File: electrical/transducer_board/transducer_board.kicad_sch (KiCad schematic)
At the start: 89 parts, among them J1 Conn_01x04_MountingPin, J2 Conn_01x01, J3 Conn_01x01, J4 Conn_01x01, J6 Conn_01x01, J9 Conn_01x01, U1 XL62783, U2 XL62083, U3 XL62783, U4 XL62083, U5 LCMXO3L-2100E-5UWG49, U6 MIC5504-1.2YM5, U7 MIC5504-3.3YM5, U8 74LVC3G34, X1 S3D10.000000B20F30T

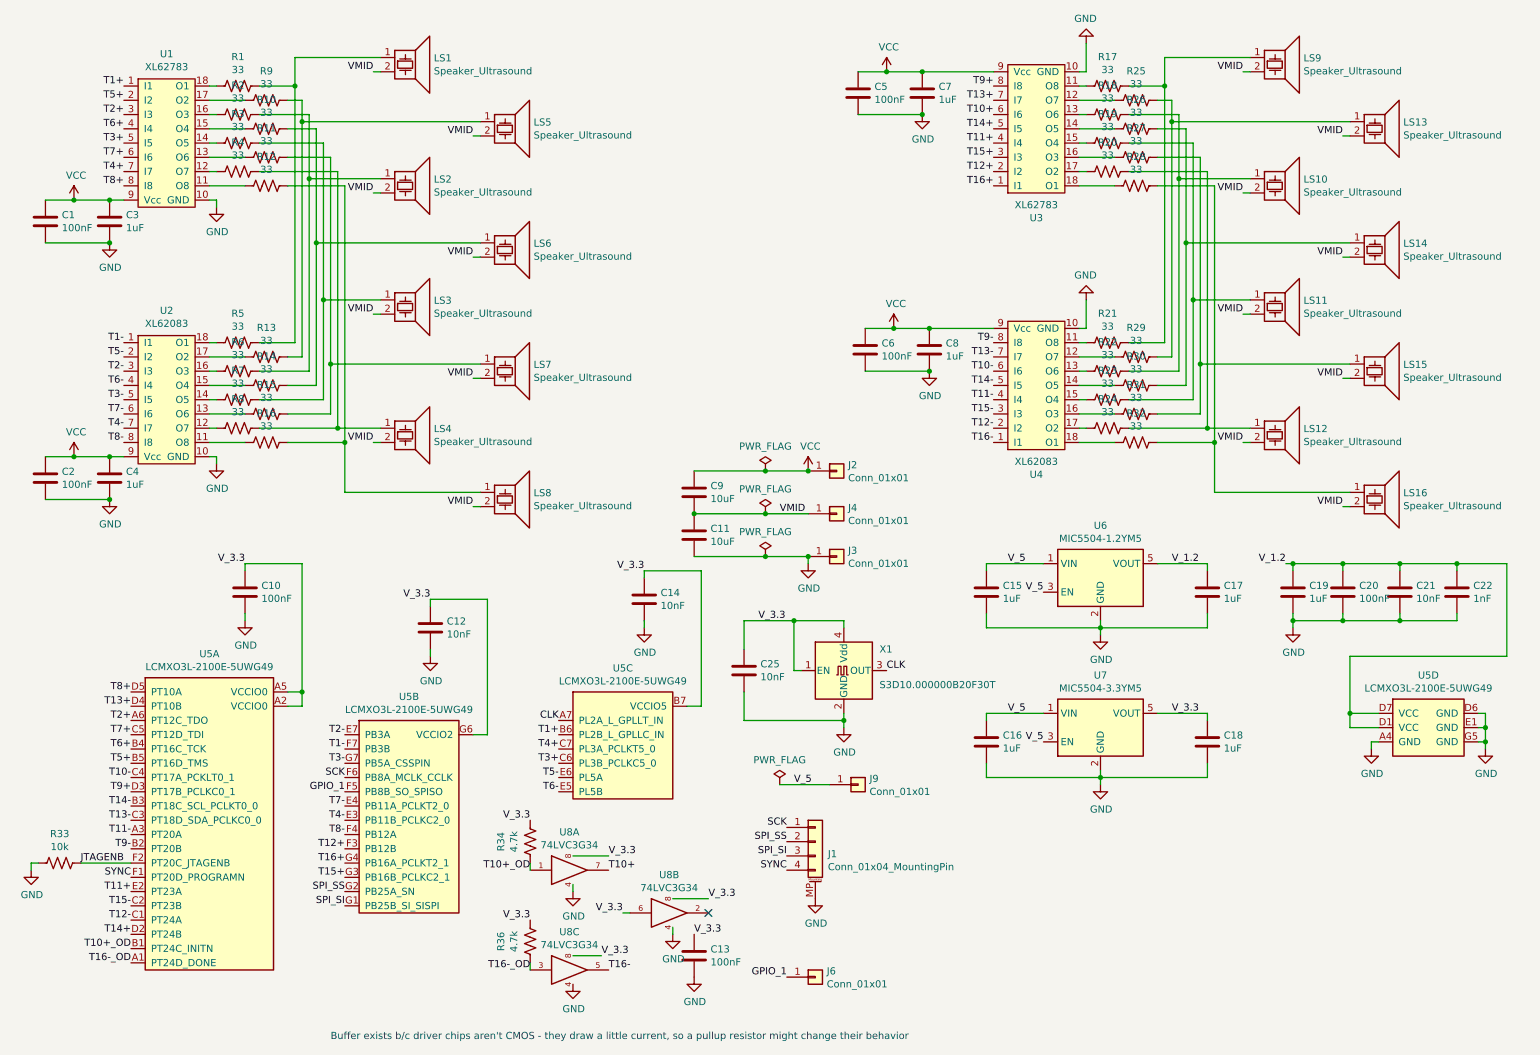
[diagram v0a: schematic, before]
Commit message: Fixed XL62083 pins and made other adjustments
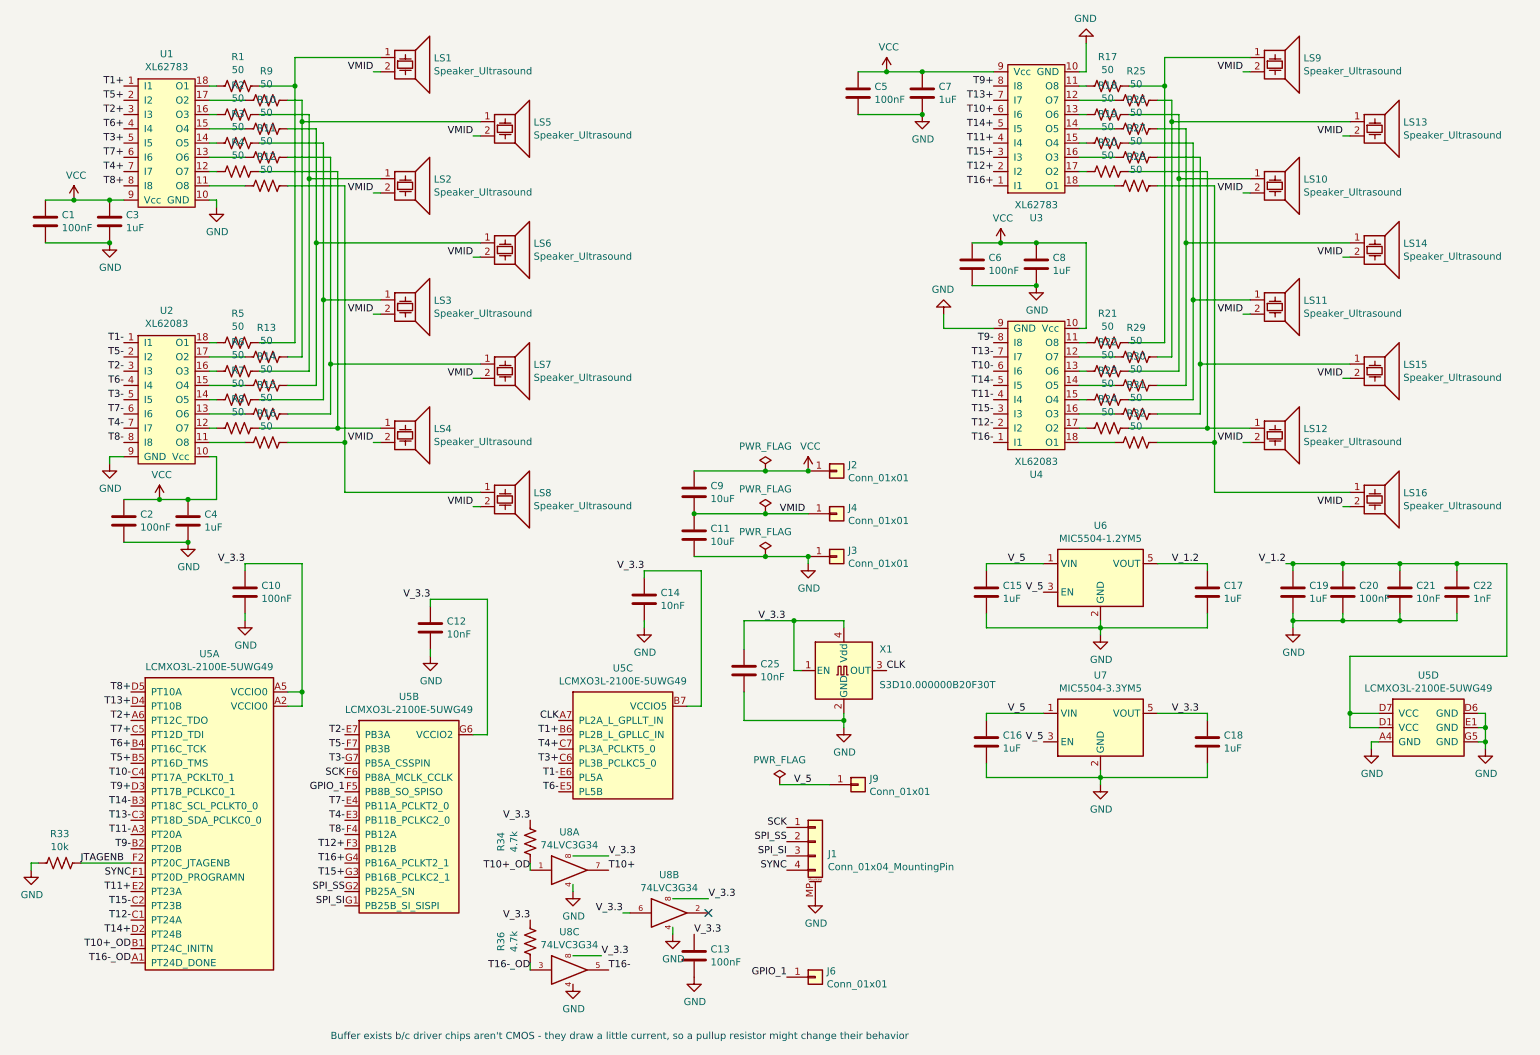
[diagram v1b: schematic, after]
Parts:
- R1, R10, R11, R12, R13, R14, R15, R16, R17, R18, R19, R2, R20, R21, R22, R23, R24, R25, R26, R27, R28, R29, R3, R30, R31, R32, R4, R5, R6, R7, R8, R9: value 33 -> 50
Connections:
- net GND: now also U2.9 (GND), U4.9 (GND); no longer U2.10 (GND), U4.10 (GND)
- net T1-: now also U5.E6 (PL5A); no longer U5.F7 (PB3B)
- net T5-: now also U5.F7 (PB3B); no longer U5.E6 (PL5A)
- net VCC: now also U2.10 (Vcc), U4.10 (Vcc); no longer U2.9 (Vcc), U4.9 (Vcc)
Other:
- moved on the sheet: C2, C4, C6, C8

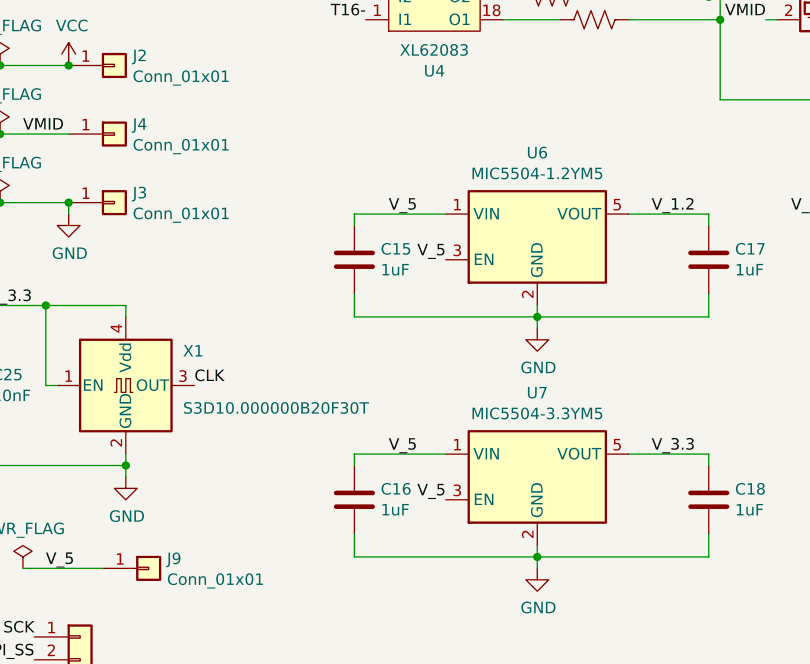
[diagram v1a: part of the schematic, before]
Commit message: Swapped some parts
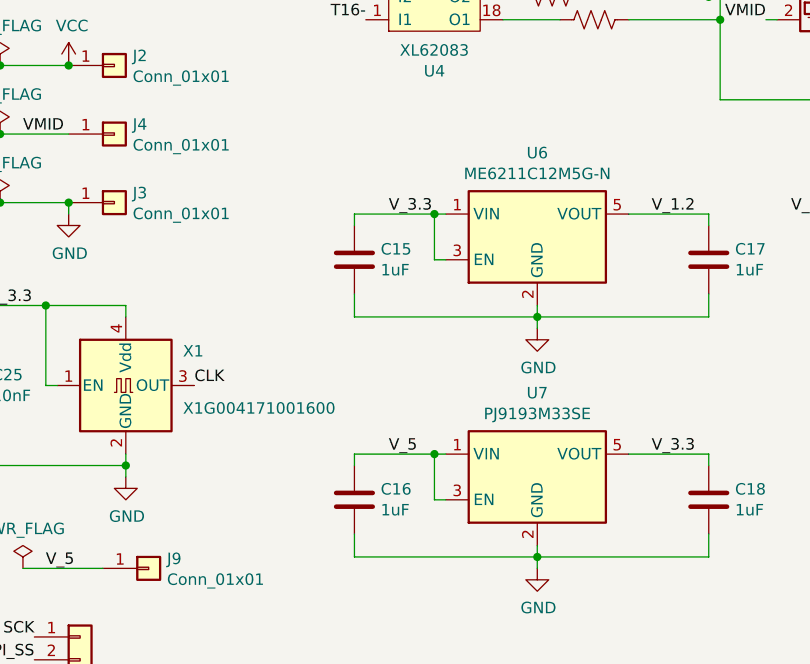
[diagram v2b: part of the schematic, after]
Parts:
- U6: value MIC5504-1.2YM5 -> ME6211C12M5G-N
- U7: value MIC5504-3.3YM5 -> PJ9193M33SE
- X1: value S3D10.000000B20F30T -> X1G004171001600; footprint Oscillator:Oscillator_SMD_Abracon_ASE-4Pin_3.2x2.5mm -> Oscillator:Oscillator_SMD_SeikoEpson_SG210-4Pin_2.5x2.0mm
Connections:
- net V_3.3: now also C15.1, U6.1 (VIN), U6.3 (EN)
- net V_5: no longer C15.1, U6.1 (VIN), U6.3 (EN)
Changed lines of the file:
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@@
   (junction (at 133.35 111.76) (diameter 0) (color 0 0 0 0)
   )
+  (junction (at 194.31 120.65) (diameter 0) (color 0 0 0 0)
+  )
   (junction (at 224.79 96.52) (diameter 0) (color 0 0 0 0)
   )
@@
   (junction (at 43.18 116.84) (diameter 0) (color 0 0 0 0)
   )
+  (junction (at 194.31 147.32) (diameter 0) (color 0 0 0 0)
+  )
   (junction (at 173.99 40.64) (diameter 0) (color 0 0 0 0)
   )
@@
     (stroke (width 0) (type default) (color 0 0 0 0))
   )
+  (wire (pts (xy 194.31 147.32) (xy 194.31 152.4))
+    (stroke (width 0) (type default) (color 0 0 0 0))
+  )
   (wire (pts (xy 64.77 52.07) (xy 77.47 52.07))
     (stroke (width 0) (type default) (color 0 0 0 0))
@@
     (stroke (width 0) (type default) (color 0 0 0 0))
   )
+  (wire (pts (xy 194.31 152.4) (xy 195.58 152.4))
+    (stroke (width 0) (type default) (color 0 0 0 0))
+  )
   (wire (pts (xy 146.05 119.38) (xy 153.67 119.38))
     (stroke (width 0) (type default) (color 0 0 0 0))
@@
     (stroke (width 0) (type default) (color 0 0 0 0))
   )
+  (wire (pts (xy 194.31 120.65) (xy 185.42 120.65))
+    (stroke (width 0) (type default) (color 0 0 0 0))
+  )
   (wire (pts (xy 250.19 66.04) (xy 248.92 66.04))
     (stroke (width 0) (type default) (color 0 0 0 0))
@@
     (stroke (width 0) (type default) (color 0 0 0 0))
   )
+  (wire (pts (xy 194.31 125.73) (xy 195.58 125.73))
+    (stroke (width 0) (type default) (color 0 0 0 0))
+  )
   (wire (pts (xy 223.52 93.98) (xy 223.52 85.09))
     (stroke (width 0) (type default) (color 0 0 0 0))
@@
     (stroke (width 0) (type default) (color 0 0 0 0))
   )
+  (wire (pts (xy 194.31 120.65) (xy 194.31 125.73))
+    (stroke (width 0) (type default) (color 0 0 0 0))
+  )
   (wire (pts (xy 162.56 33.02) (xy 167.64 33.02))
     (stroke (width 0) (type default) (color 0 0 0 0))
@@
     (stroke (width 0) (type default) (color 0 0 0 0))
   )
-  (wire (pts (xy 195.58 120.65) (xy 185.42 120.65))
+  (wire (pts (xy 195.58 120.65) (xy 194.31 120.65))
     (stroke (width 0) (type default) (color 0 0 0 0))
   )
@@
     (stroke (width 0) (type default) (color 0 0 0 0))
   )
-  (wire (pts (xy 185.42 147.32) (xy 195.58 147.32))
+  (wire (pts (xy 185.42 147.32) (xy 194.31 147.32))
     (stroke (width 0) (type default) (color 0 0 0 0))
   )
@@
     (stroke (width 0) (type default) (color 0 0 0 0))
   )
+  (wire (pts (xy 194.31 147.32) (xy 195.58 147.32))
+    (stroke (width 0) (type default) (color 0 0 0 0))
+  )
   (wire (pts (xy 111.76 179.07) (xy 111.76 177.8))
     (stroke (width 0) (type default) (color 0 0 0 0))
@@
     (effects (font (size 1.27 1.27)) (justify right bottom))
   )
-  (label "V_5" (at 189.23 120.65 0)
+  (label "V_3.3" (at 189.23 120.65 0)
     (effects (font (size 1.27 1.27)) (justify left bottom))
   )
@@
     (effects (font (size 1.27 1.27)) (justify right bottom))
   )
-  (label "V_5" (at 195.58 152.4 180)
-    (effects (font (size 1.27 1.27)) (justify right bottom))
-  )
   (label "T10-" (at 186.69 86.36 180)
     (effects (font (size 1.27 1.27)) (justify right bottom))
@@
     (effects (font (size 1.27 1.27)) (justify right bottom))
   )
-  (label "V_5" (at 195.58 125.73 180)
-    (effects (font (size 1.27 1.27)) (justify right bottom))
-  )
   (label "T14+" (at 186.69 43.18 180)
     (effects (font (size 1.27 1.27)) (justify right bottom))
@@
     (in_bom yes) (on_board yes)
     (property "Reference" "U6" (id 0) (at 205.74 113.8682 0))
-    (property "Value" "MIC5504-1.2YM5" (id 1) (at 205.74 116.1796 0))
+    (property "Value" "ME6211C12M5G-N" (id 1) (at 205.74 116.1796 0))
     (property "Footprint" "Package_TO_SOT_SMD:SOT-23-5" (id 2) (at 205.74 133.35 0)
       (effects (font (size 1.27 1.27)) hide)
@@
     (in_bom yes) (on_board yes)
     (property "Reference" "U7" (id 0) (at 205.74 140.5382 0))
-    (property "Value" "MIC5504-3.3YM5" (id 1) (at 205.74 142.8496 0))
+    (property "Value" "PJ9193M33SE" (id 1) (at 205.74 142.8496 0))
     (property "Footprint" "Package_TO_SOT_SMD:SOT-23-5" (id 2) (at 205.74 160.02 0)
       (effects (font (size 1.27 1.27)) hide)
@@
       (effects (font (size 1.27 1.27)) (justify left))
     )
-    (property "Value" "S3D10.000000B20F30T" (id 1) (at 166.37 142.24 0)
+    (property "Value" "X1G004171001600" (id 1) (at 166.37 142.24 0)
       (effects (font (size 1.27 1.27)) (justify left))
     )
-    (property "Footprint" "Oscillator:Oscillator_SMD_Abracon_ASE-4Pin_3.2x2.5mm" (id 2) (at 177.8 148.59 0)
+    (property "Footprint" "Oscillator:Oscillator_SMD_SeikoEpson_SG210-4Pin_2.5x2.0mm" (id 2) (at 177.8 148.59 0)
       (effects (font (size 1.27 1.27)) hide)
     )
@@
     )
     (path "/00000000-0000-0000-0000-0000613404e8"
-      (reference "U6") (unit 1) (value "MIC5504-1.2YM5") (footprint "Package_TO_SOT_SMD:SOT-23-5")
+      (reference "U6") (unit 1) (value "ME6211C12M5G-N") (footprint "Package_TO_SOT_SMD:SOT-23-5")
     )
     (path "/00000000-0000-0000-0000-00006134175c"
-      (reference "U7") (unit 1) (value "MIC5504-3.3YM5") (footprint "Package_TO_SOT_SMD:SOT-23-5")
+      (reference "U7") (unit 1) (value "PJ9193M33SE") (footprint "Package_TO_SOT_SMD:SOT-23-5")
     )
     (path "/00000000-0000-0000-0000-000061572b7c"
@@
     )
     (path "/00000000-0000-0000-0000-00006168392e"
-      (reference "X1") (unit 1) (value "S3D10.000000B20F30T") (footprint "Oscillator:Oscillator_SMD_Abracon_ASE-4Pin_3.2x2.5mm")
+      (reference "X1") (unit 1) (value "X1G004171001600") (footprint "Oscillator:Oscillator_SMD_SeikoEpson_SG210-4Pin_2.5x2.0mm")
     )
   )

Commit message: Add a few components
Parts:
- added C23, C24, C26, C27, C28, C29: (no value), symbol Device:C
- added D1, D2: (no value), symbol Device:D
- C1, C10, C13, C2, C20, C5, C6: value 100nF -> (none); footprint Capacitor_SMD:C_0603_1608Metric -> (none)
- C11, C9: value 10uF -> (none); footprint Capacitor_SMD:C_0805_2012Metric -> (none)
- C12, C14, C25: value 10nF -> (none); footprint Capacitor_SMD:C_0402_1005Metric -> (none)
- C15, C16, C17, C18, C19, C3, C4, C7, C8: value 1uF -> (none); footprint Capacitor_SMD:C_0603_1608Metric -> (none)
- C21: value 10nF -> (none); footprint Capacitor_SMD:C_0603_1608Metric_Pad1.08x0.95mm_HandSolder -> (none)
- C22: value 1nF -> (none); footprint Capacitor_SMD:C_0603_1608Metric_Pad1.08x0.95mm_HandSolder -> (none)
- J1: value Conn_01x04_MountingPin -> (none); footprint Connector_JST:JST_SH_BM04B-SRSS-TB_1x04-1MP_P1.00mm_Vertical -> (none)
- J2, J3, J4, J9: value Conn_01x01 -> (none); footprint Connector_Pin:Pin_D1.3mm_L11.0mm -> (none)
- J6: value Conn_01x01 -> (none); footprint Connector_Pin:Pin_D1.0mm_L10.0mm -> (none)
- LS1, LS10, LS11, LS12, LS13, LS14, LS15, LS16, LS2, LS3, LS4, LS5, LS6, LS7, LS8, LS9: value Speaker_Ultrasound -> (none); footprint Ultrasonic Emitters:Ultrasonic_Transducer_T40-16 -> (none)
- R1, R10, R11, R12, R13, R14, R15, R16, R17, R18, R19, R2, R20, R21, R22, R23, R24, R25, R26, R27, R28, R29, R3, R30, R31, R32, R4, R5, R6, R7, R8, R9: value 50 -> (none); footprint Resistor_SMD:R_1206_3216Metric -> (none)
- R33: value 10k -> (none); footprint Resistor_SMD:R_0603_1608Metric -> (none)
- R34, R36: value 4.7k -> (none); footprint Resistor_SMD:R_0402_1005Metric -> (none)
- U1, U3: value XL62783 -> (none); footprint Ultrasonic Emitters:SOIC-18W_7.5x11.6mm_P1.27mm_Weird -> (none)
- U2, U4: value XL62083 -> (none); footprint Ultrasonic Emitters:SOIC-18W_7.5x11.6mm_P1.27mm_Weird -> (none)
- U5: value LCMXO3L-2100E-5UWG49 -> (none); footprint Package_CSP:ST_WLCSP-49_Die433 -> (none)
- U6: value ME6211C12M5G-N -> (none); footprint Package_TO_SOT_SMD:SOT-23-5 -> (none)
- U7: value PJ9193M33SE -> (none); footprint Package_TO_SOT_SMD:SOT-23-5 -> (none)
- U8: value 74LVC3G34 -> (none); footprint Package_SO:VSSOP-8_2.3x2mm_P0.5mm -> (none)
- X1: value X1G004171001600 -> (none); footprint Oscillator:Oscillator_SMD_SeikoEpson_SG210-4Pin_2.5x2.0mm -> (none)
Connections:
- net GND: now also C23.2, C24.2, C27.2, C28.2, C29.2; no longer C1.2, C3.2, C5.2, C7.2
- net VCC: now also C23.1, C24.1, C26.1, C28.1, C29.1; no longer C2.1, C4.1, C6.1, C8.1
- net VMID: now also C1.2, C2.1, C3.2, C4.1, C5.2, C6.1, C7.2, C8.1, C26.2, C27.1
- net V_3.3: now also D2.2 (A); no longer C15.1, U6.1 (VIN), U6.3 (EN)
- net V_5: now also D1.2 (A); no longer C16.1, U7.1 (VIN), U7.3 (EN)
- new net V_3.3_D: C15.1, D2.1 (K), U6.1 (VIN), U6.3 (EN)
- new net V_5_D: C16.1, D1.1 (K), U7.1 (VIN), U7.3 (EN)
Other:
- moved on the sheet: C1, C10, C11, C12, C13, C14, C15, C16, C17, C18, C19, C2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
